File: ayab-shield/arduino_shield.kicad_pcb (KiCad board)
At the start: 2 copper layers, 68.6 x 53.3 mm, 30 parts, among them IC1 ULN2803A, IC2 ULN2803A, IC3 MCP2300X/P, IC4 MCP2300X/P, J1 Power, J2 Digital/PWM, J3 Analog, J4 Digital/PWM, X1 KLDX-0202-AC

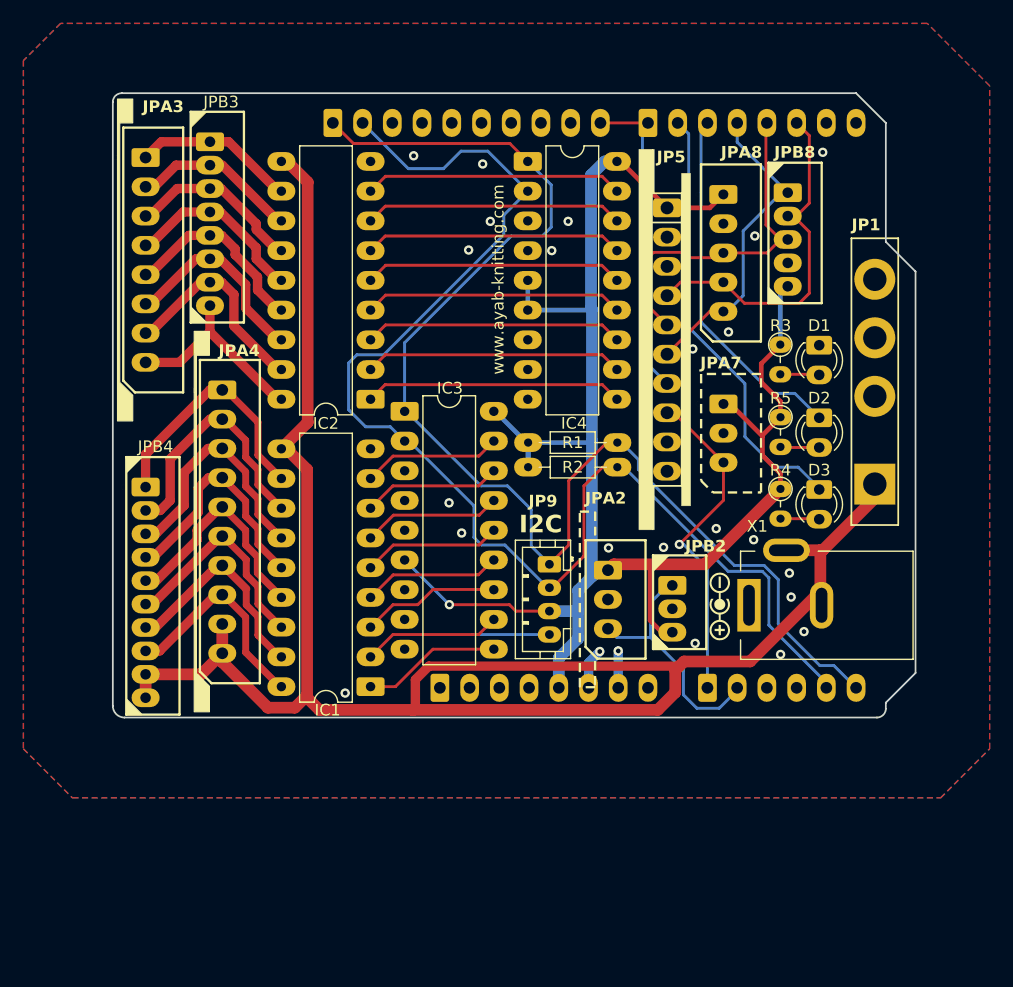
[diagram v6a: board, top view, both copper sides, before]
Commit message: Add shield logo and version
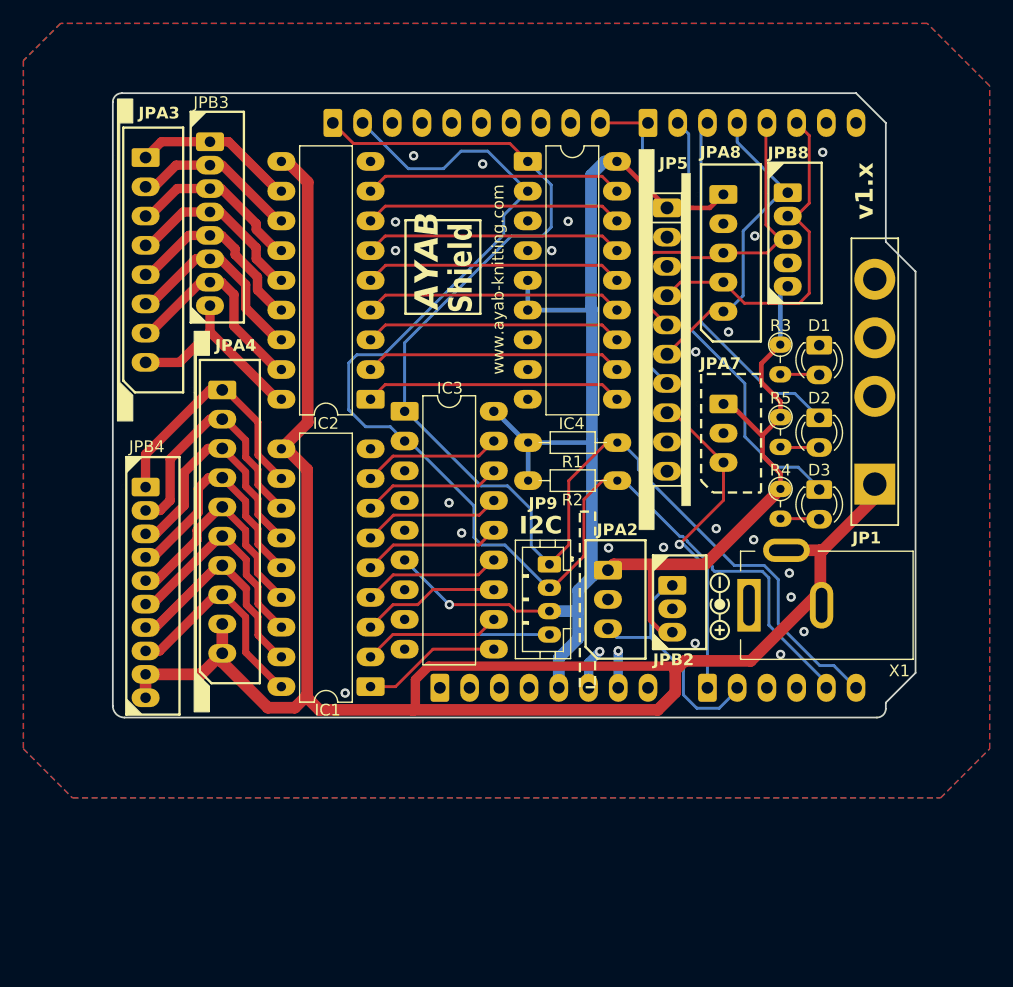
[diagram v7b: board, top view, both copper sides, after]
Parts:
- moved R2 1.15 mm to (157.8, 109.8)
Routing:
- net /SDA: track 111.2 -> 109.7 mm
- net +5V: track 148.8 -> 147.8 mm
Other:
- board text added: "AYAB"
- board text added: "Shield"
- board text added: "v1.x"
